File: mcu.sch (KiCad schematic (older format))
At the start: 14 parts, among them J3 Conn_ARM_JTAG_SWD_10, SW1 SW_MEC_5E, SW2 SW_MEC_5E, U6 STM32F070CBTx, Y1 12MHz

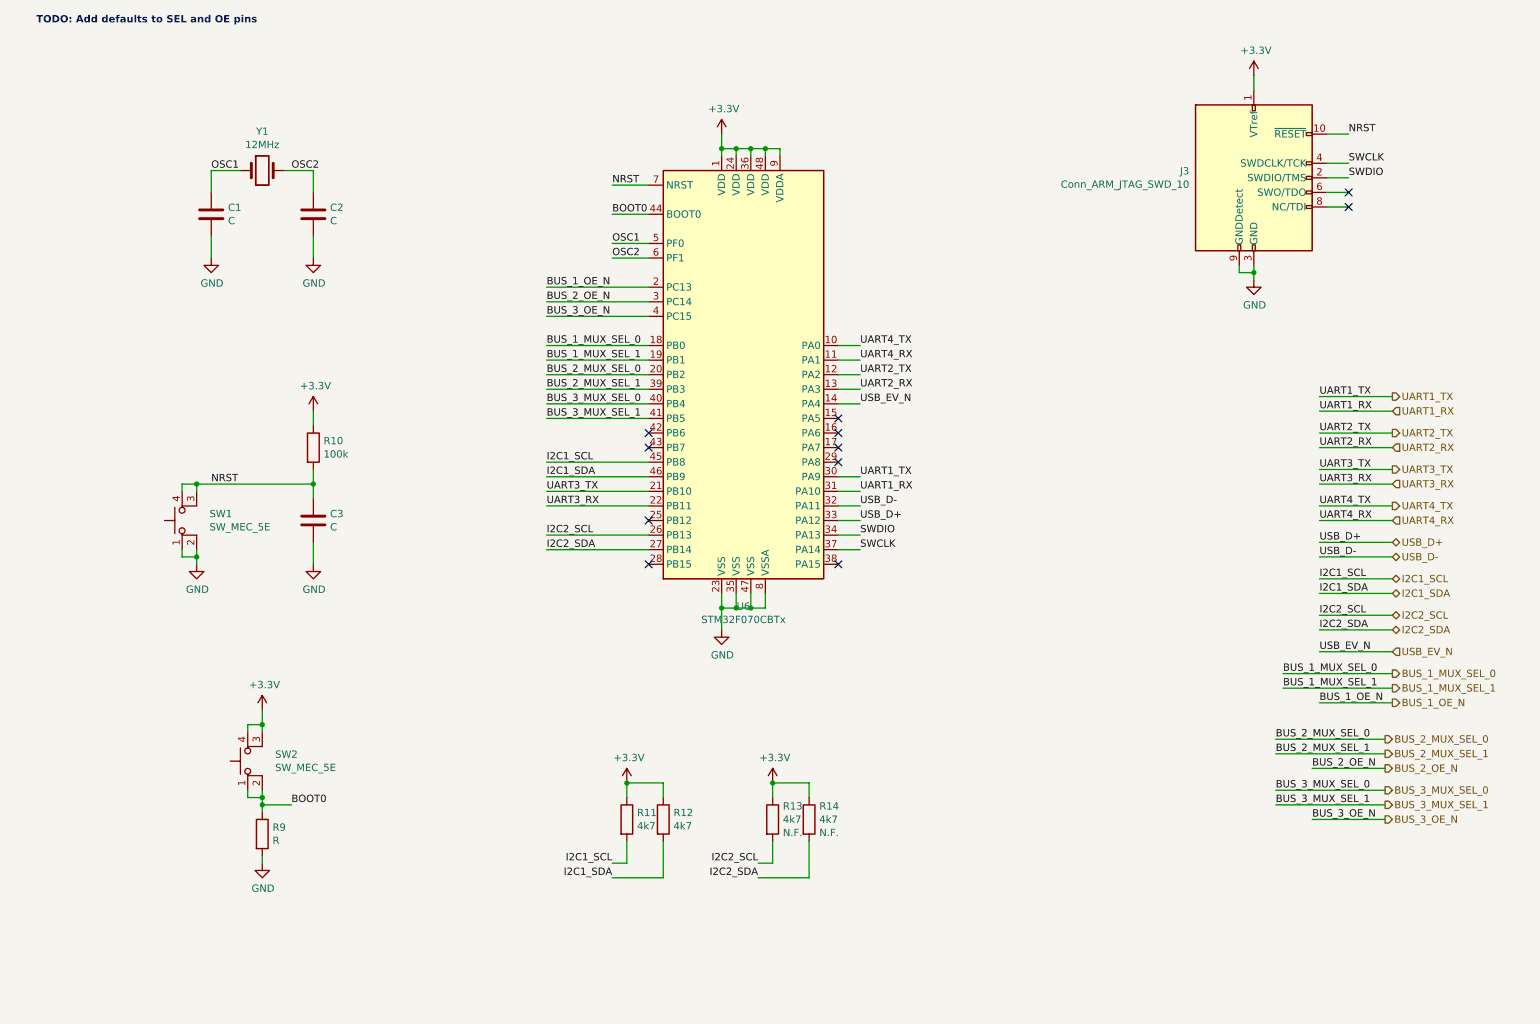
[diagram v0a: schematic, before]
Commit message: Complete muxing and level translation
Added Aux USB to avoid using a HUB, which don't seem to be too readily
available out there and would complicate the design for no good reason.

Now the i2c lines can also be switched.

Added voltage level translation up to 1.2V from 3.3V. Selected
bidirectional level translator.

Started looking into power supply.
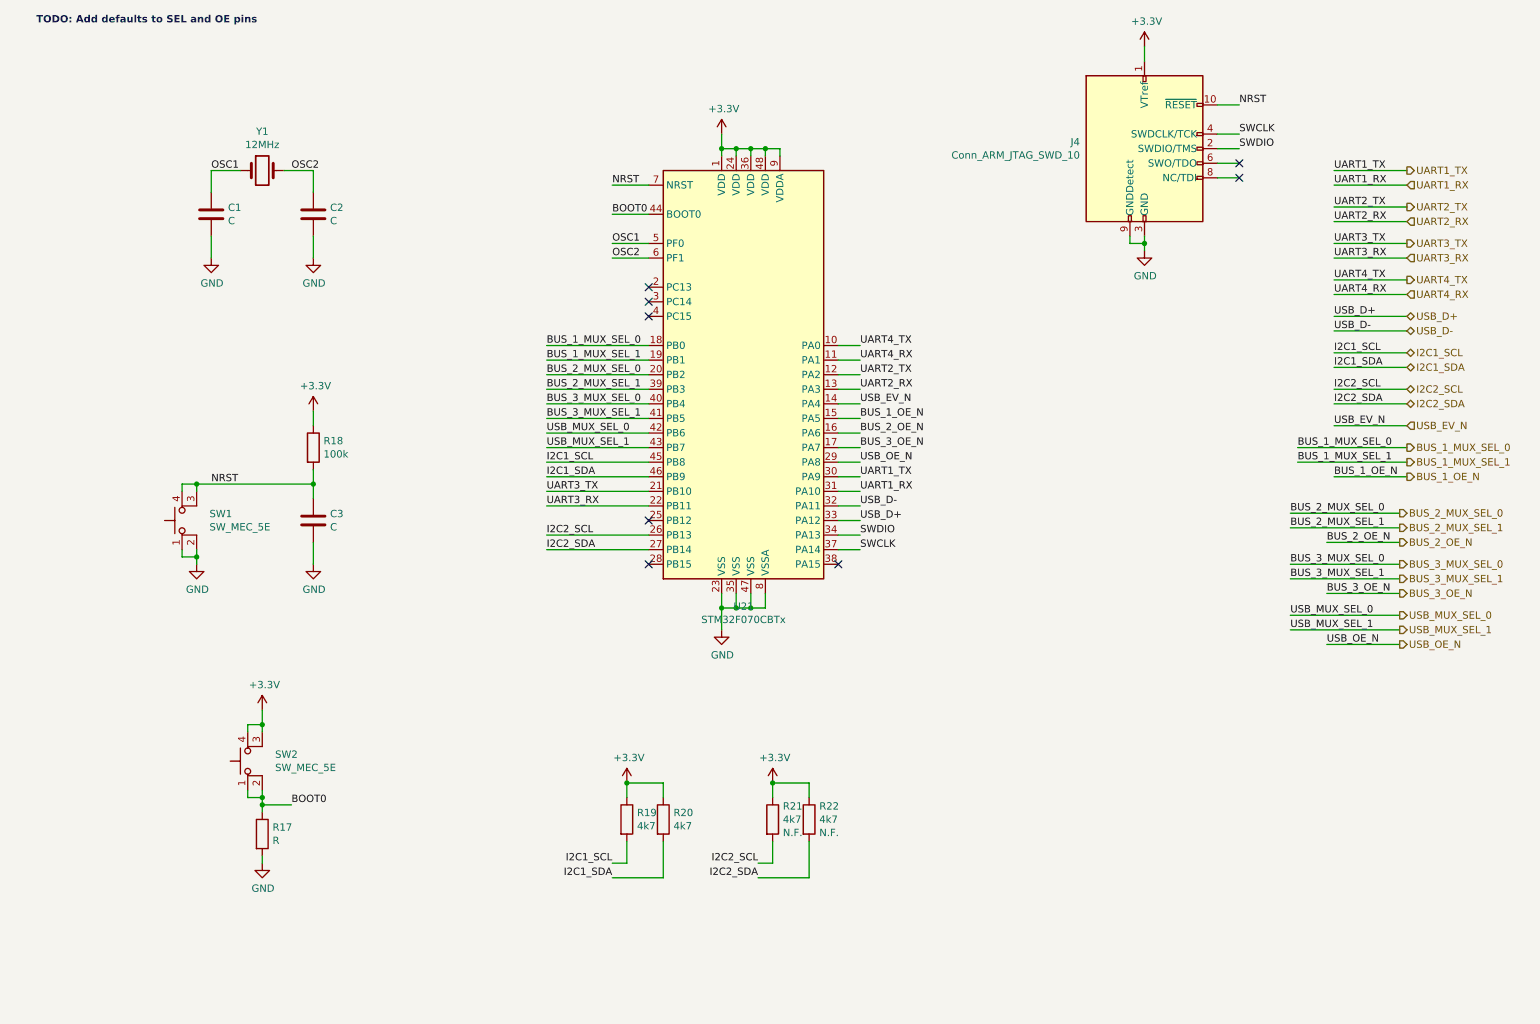
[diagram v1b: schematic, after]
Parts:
- renumbered J3 to J4, R9 to R17, R10 to R18, R11 to R19, R12 to R20, R13 to R21, R14 to R22, U6 to U21
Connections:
- net BUS_1_OE_N: now also U21.15 (PA5); no longer U21.2 (PC13)
- net BUS_2_OE_N: now also U21.16 (PA6); no longer U21.3 (PC14)
- net BUS_3_OE_N: now also U21.17 (PA7); no longer U21.4 (PC15)
- net USB_OE_N: now reaches U21.29 (PA8)
- net USB_MUX_SEL_0: now reaches U21.42 (PB6)
- net USB_MUX_SEL_1: now reaches U21.43 (PB7)
- no-connect marks 11 -> 8
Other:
- moved on the sheet: J4

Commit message: Supply caps, initial signal states and headers
  * Added bulk supply caps.
  * Set initial control signal states via resistors.
  * Add debug headers.
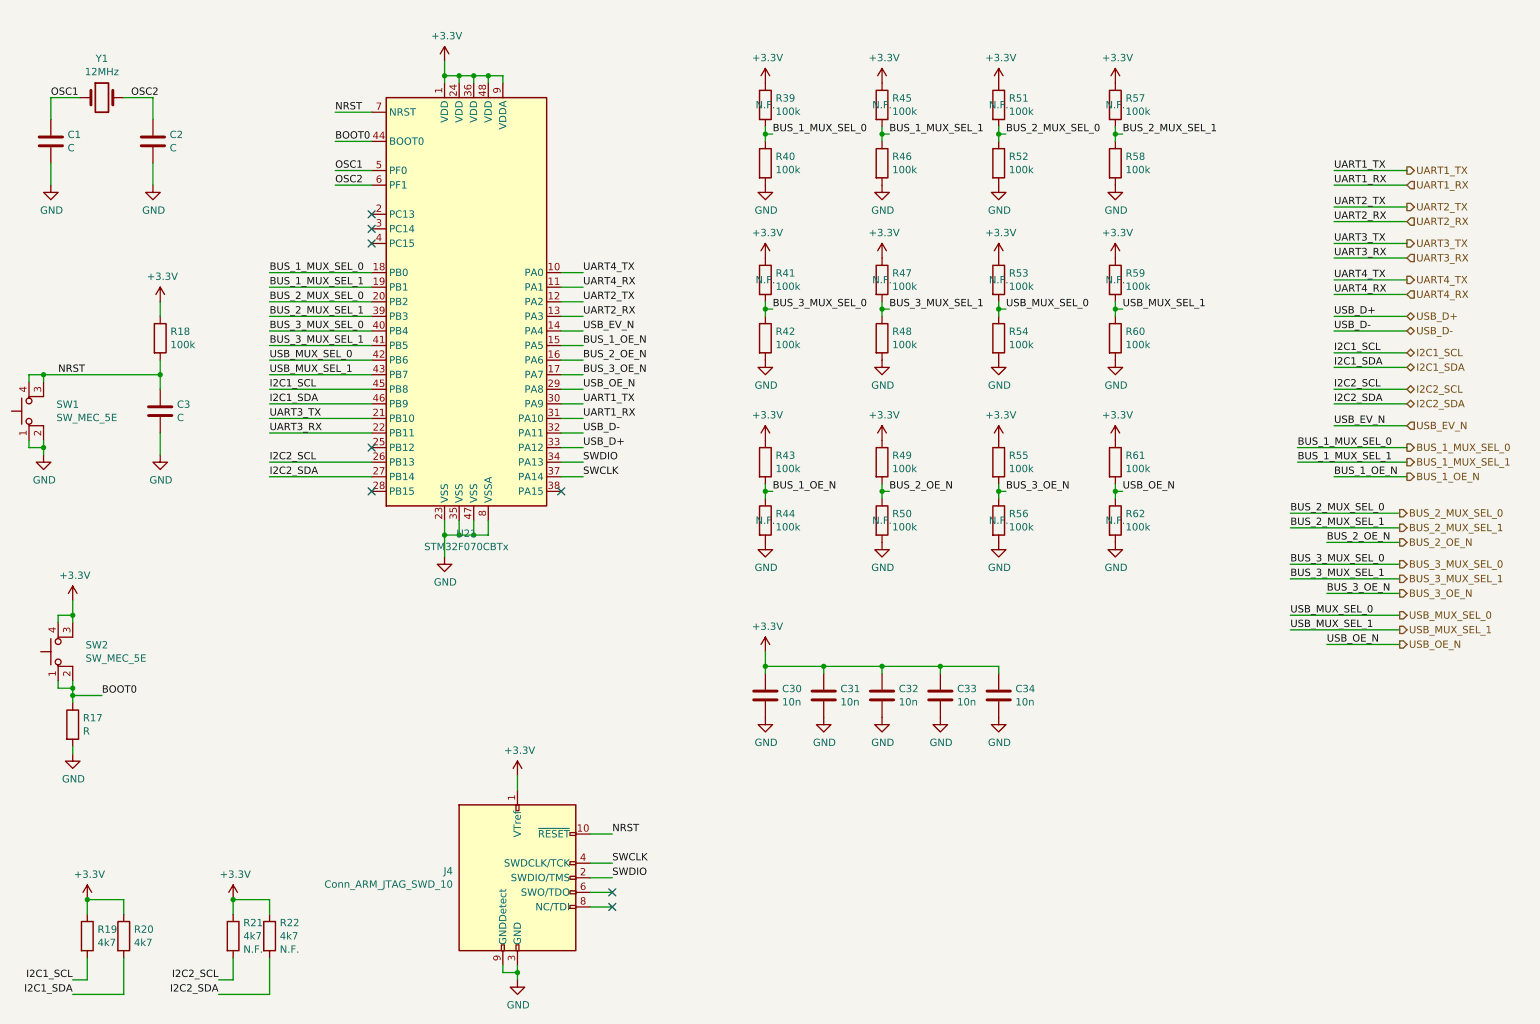
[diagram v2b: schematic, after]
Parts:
- added C30, C31, C32, C33, C34: 10n, symbol Device:C
- added R39, R40, R41, R42, R43, R44, R45, R46, R47, R48, R49, R50, R51, R52, R53, R54, R55, R56, R57, R58, R59, R60, R61, R62: 100k, symbol Device:R
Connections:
- net +3V3: now also C30.1, C31.1, C32.1, C33.1, C34.1, R39.1, R41.1, R43.1, R45.1, R47.1, R49.1, R51.1, R53.1, R55.1, R57.1, R59.1, R61.1
- net BUS_1_MUX_SEL_0: now also R39.2, R40.1
- net BUS_1_MUX_SEL_1: now also R45.2, R46.1
- net BUS_1_OE_N: now also R43.2, R44.1
- net BUS_2_MUX_SEL_0: now also R51.2, R52.1
- net BUS_2_MUX_SEL_1: now also R57.2, R58.1
- net BUS_2_OE_N: now also R49.2, R50.1
- net BUS_3_MUX_SEL_0: now also R41.2, R42.1
- net BUS_3_MUX_SEL_1: now also R47.2, R48.1
- net BUS_3_OE_N: now also R55.2, R56.1
- net GND: now also C30.2, C31.2, C32.2, C33.2, C34.2, R40.2, R42.2, R44.2, R46.2, R48.2, R50.2, R52.2, R54.2, R56.2, R58.2, R60.2, R62.2
- net USB_MUX_SEL_0: now also R53.2, R54.1
- net USB_MUX_SEL_1: now also R59.2, R60.1
- net USB_OE_N: now also R61.2, R62.1
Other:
- note removed: "TODO: Add defaults to SEL and OE pins"
- moved on the sheet: C1, C2, C3, J4, R17, R18, R19, R20, R21, R22, SW1, SW2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

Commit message: Replace MCU by something available in distributors
Given the current chip shortage the STM32F0 was not available from
JLCPCB. This one (STM32F411CE) is available in large quantities from
JLCPCB. Despite being much more powerful than the F0, it is still in the
price range and actually cheaper than the STM32F103C8T6... which I don't
understand...
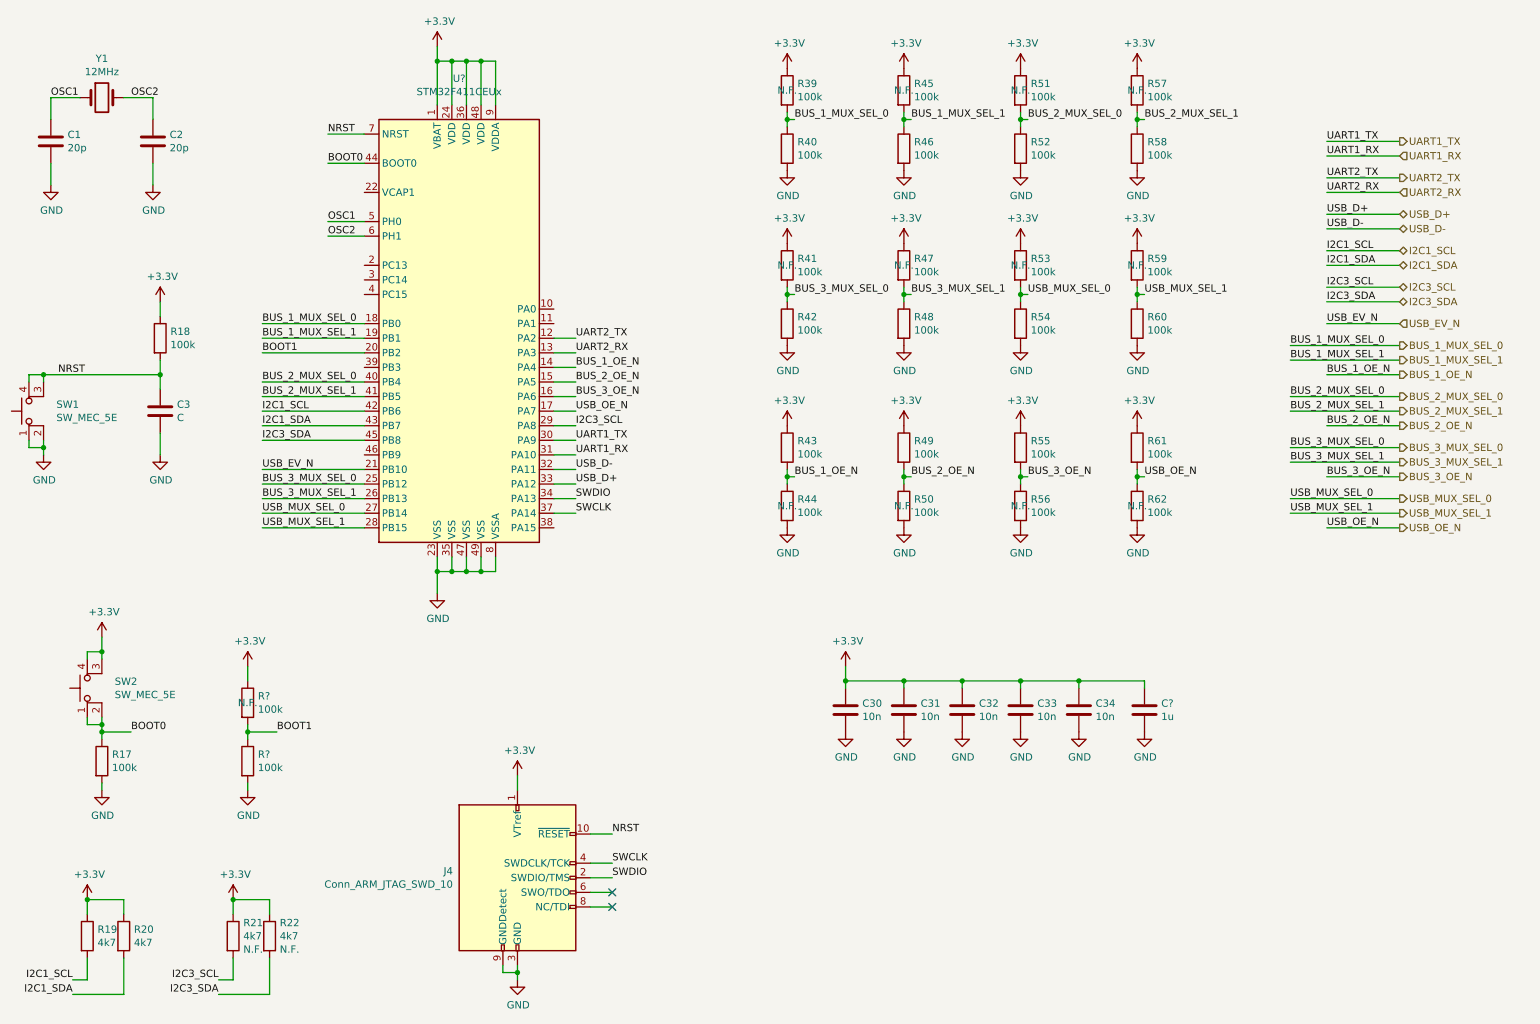
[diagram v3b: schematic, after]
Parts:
- removed U21: STM32F070CBTx, Package_QFP:LQFP-48_7x7mm_P0.5mm, symbol MCU_ST_STM32F0:STM32F070CBTx
- added C?: 1u, symbol Device:C
- added R? (x2): 100k, symbol Device:R
- added U?: STM32F411CEUx, Package_DFN_QFN:QFN-48-1EP_7x7mm_P0.5mm_EP5.6x5.6mm, symbol MCU_ST_STM32F4:STM32F411CEUx
- C1, C2: value C -> 20p
- R17: value R -> 100k
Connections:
- net +3V3: now also C?.1, R?.1, U?.1 (VBAT), U?.24 (VDD), U?.36 (VDD), U?.48 (VDD), U?.9 (VDDA)
- net BOOT0: now also U?.44 (BOOT0)
- net BUS_1_MUX_SEL_0: now also U?.18 (PB0)
- net BUS_1_MUX_SEL_1: now also U?.19 (PB1)
- net BUS_1_OE_N: now also U?.14 (PA4)
- net BUS_2_MUX_SEL_0: now also U?.40 (PB4)
- net BUS_2_MUX_SEL_1: now also U?.41 (PB5)
- net BUS_2_OE_N: now also U?.15 (PA5)
- net BUS_3_MUX_SEL_0: now also U?.25 (PB12)
- net BUS_3_MUX_SEL_1: now also U?.26 (PB13)
- net BUS_3_OE_N: now also U?.16 (PA6)
- net GND: now also C?.2, R?.2, U?.23 (VSS), U?.35 (VSS), U?.47 (VSS), U?.49 (VSS), U?.8 (VSSA)
- net I2C1_SCL: now also U?.42 (PB6)
- net I2C1_SDA: now also U?.43 (PB7)
- net NRST: now also U?.7 (NRST)
- net OSC1: now also U?.5 (PH0)
- net OSC2: now also U?.6 (PH1)
- net SWCLK: now also U?.37 (PA14)
- net SWDIO: now also U?.34 (PA13)
- net UART1_RX: now also U?.31 (PA10)
- net UART1_TX: now also U?.30 (PA9)
- net UART2_RX: now also U?.13 (PA3)
- net UART2_TX: now also U?.12 (PA2)
- net USB_D+: now also U?.33 (PA12)
- net USB_D-: now also U?.32 (PA11)
- net USB_EV_N: now also U?.21 (PB10)
- net USB_MUX_SEL_0: now also U?.27 (PB14)
- net USB_MUX_SEL_1: now also U?.28 (PB15)
- net USB_OE_N: now also U?.17 (PA7)
- net I2C2_SCL renamed I2C3_SCL
- net I2C3_SCL: now also U?.29 (PA8)
- net I2C2_SDA renamed I2C3_SDA
- net I2C3_SDA: now also U?.45 (PB8)
- new net BOOT1: R?.1, R?.2, U?.20 (PB2)
- no-connect marks 8 -> 2
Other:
- moved on the sheet: C30, C31, C32, C33, C34, R17, R39, R40, R41, R42, R43, R44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
